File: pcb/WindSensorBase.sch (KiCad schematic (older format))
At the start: 8 parts, among them IC1 MCP2562FD, P1 CONN_4, U1 JDY40, U2 DCDCConverter, U3 ESP32Dev

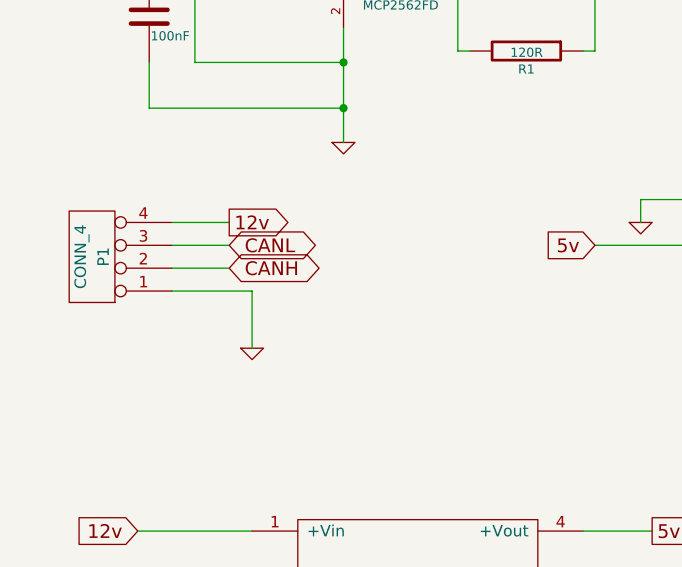
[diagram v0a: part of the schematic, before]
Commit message: Fixed 49day overflows
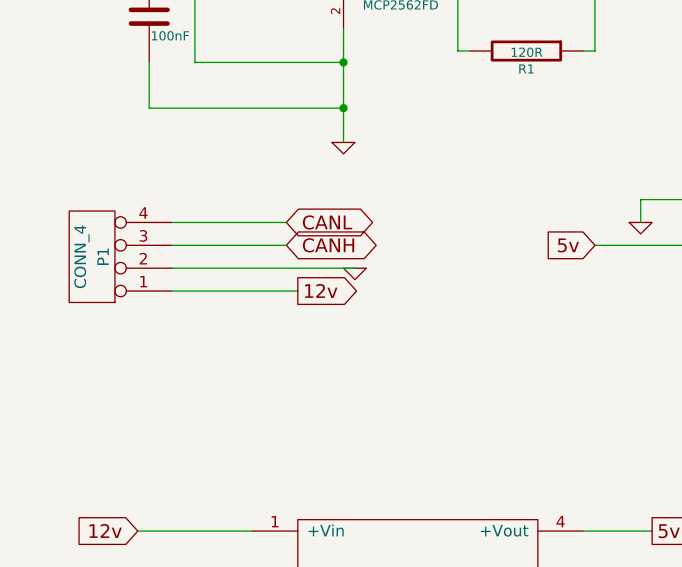
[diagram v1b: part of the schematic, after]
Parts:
- U1: footprint Divers:JDY-40 -> Divers:JDY-40-TH
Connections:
- net 12v: now also P1.1 (P1); no longer P1.4 (P4)
- net CANH: now also P1.3 (P3); no longer P1.2 (P2)
- net CANL: now also P1.4 (P4); no longer P1.3 (P3)
- net GND: now also P1.2 (P2); no longer P1.1 (P1)
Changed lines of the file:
@@
 F 0 "U1" H 2100 2300 60  0000 C CNN
 F 1 "JDY40" H 2100 2450 60  0000 C CNN
-F 2 "Divers:JDY-40" H 1900 2400 60  0001 C CNN
+F 2 "Divers:JDY-40-TH" H 1900 2400 60  0001 C CNN
 F 3 "" H 1900 2400 60  0001 C CNN
 	1    2050 2450
@@
 Text GLabel 3150 3900 2    60   BiDi ~ 0
 CANL
-Text GLabel 1500 5250 2    60   BiDi ~ 0
+Text GLabel 1750 5150 2    60   BiDi ~ 0
 CANH
-Text GLabel 1500 5150 2    60   BiDi ~ 0
+Text GLabel 1750 5050 2    60   BiDi ~ 0
 CANL
 $Comp
 L GND #PWR08
 U 1 1 5FEC749C
-P 1600 5600
-F 0 "#PWR08" H 1600 5600 30  0001 C CNN
-F 1 "GND" H 1600 5530 30  0001 C CNN
-F 2 "" H 1600 5600 60  0001 C CNN
-F 3 "" H 1600 5600 60  0001 C CNN
-	1    1600 5600
-	1    0    0    -1
-$EndComp
-Text GLabel 1500 5050 2    60   Output ~ 0
+P 2050 5250
+F 0 "#PWR08" H 2050 5250 30  0001 C CNN
+F 1 "GND" H 2050 5180 30  0001 C CNN
+F 2 "" H 2050 5250 60  0001 C CNN
+F 3 "" H 2050 5250 60  0001 C CNN
+	1    2050 5250
+	1    0    0    -1
+$EndComp
+Text GLabel 1800 5350 2    60   Output ~ 0
 12v
 $Comp
@@
 $EndComp
 Wire Wire Line
-	1250 5350 1600 5350
-Wire Wire Line
-	1600 5350 1600 5600
-Wire Wire Line
-	1250 5250 1500 5250
-Wire Wire Line
-	1250 5150 1500 5150
-Wire Wire Line
-	1250 5050 1500 5050
+	1250 5350 1800 5350
+Wire Wire Line
+	1250 5250 2050 5250
 Wire Wire Line
 	7500 4350 7800 4350
 NoConn ~ 7500 3750
+Wire Wire Line
+	1250 5050 1750 5050
+Wire Wire Line
+	1250 5150 1750 5150
 $EndSCHEMATC
